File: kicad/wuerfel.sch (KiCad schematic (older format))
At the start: 18 parts, among them IC1 ATTINY13A-P

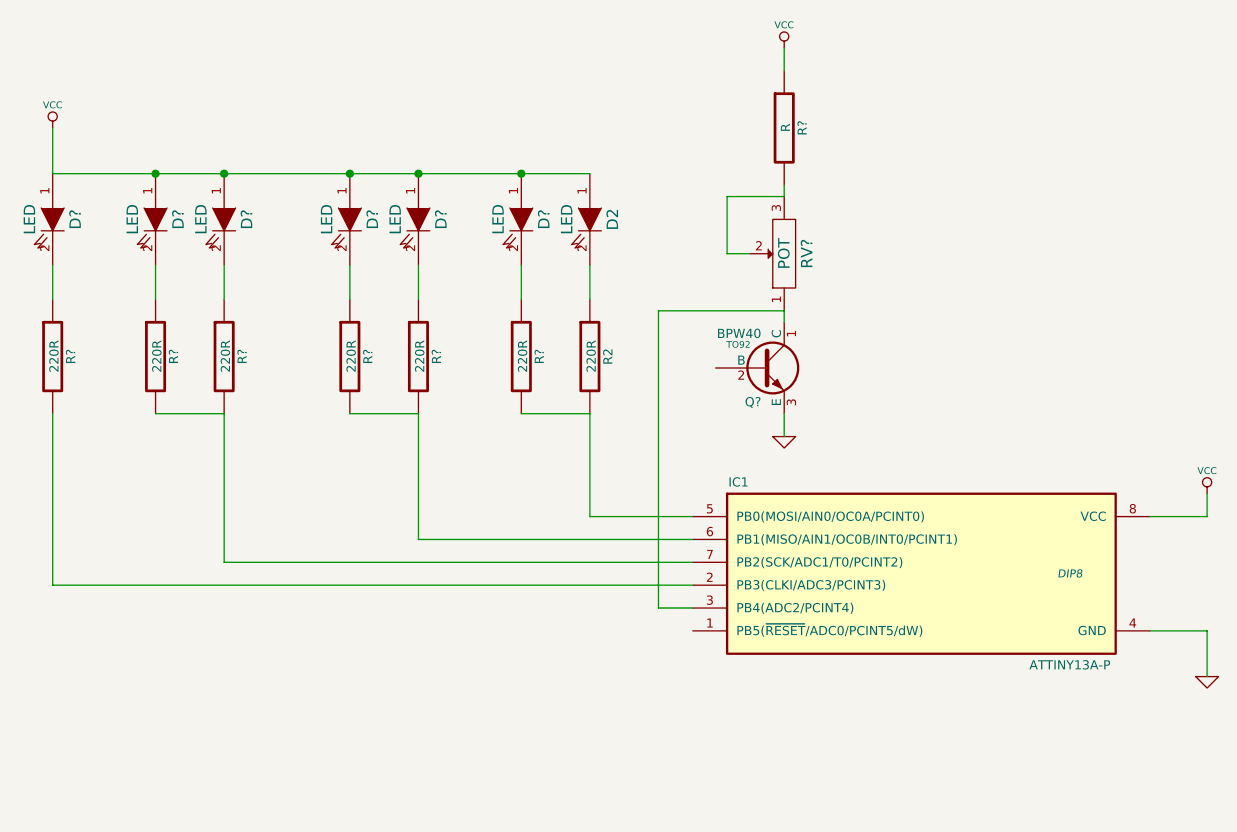
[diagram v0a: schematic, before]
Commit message: Stub für firmware angelegt, Readme erweitert
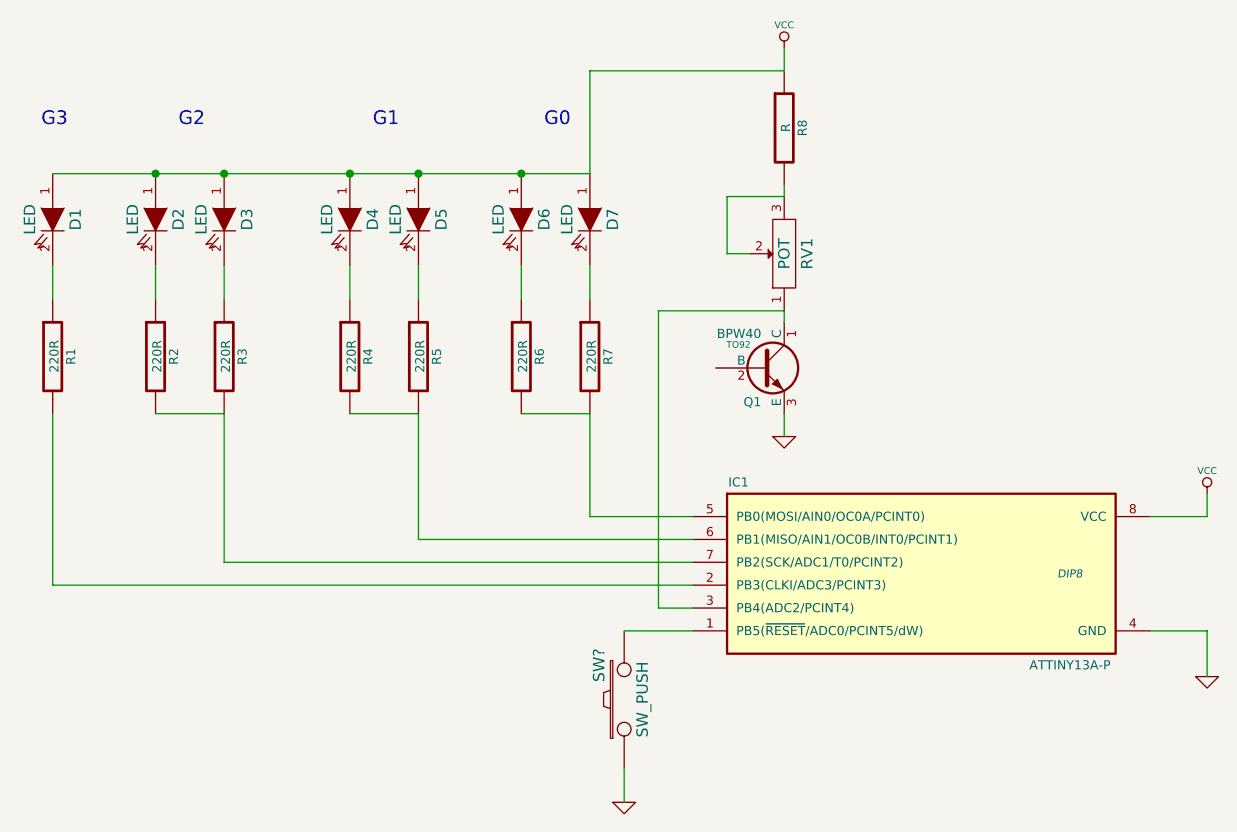
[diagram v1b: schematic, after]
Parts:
- added SW?: SW_PUSH, ~, symbol SW_PUSH
- gave numbers to parts that had none: 15
- renumbered D2 to D7, R2 to R7
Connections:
- net GND: now also SW?.1
- net at IC1.1 (PB5(~RESET~/ADC0/PCINT5/dW)): now also SW?.2
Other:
- note added: "G0"
- note added: "G1"
- note added: "G2"
- note added: "G3\n"
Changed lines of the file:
@@
 LIBS:contrib
 LIBS:valves
-LIBS:Gajda_opto
+LIBS:wuerfel-cache
 EELAYER 27 0
 EELAYER END
@@
 Sheet 1 1
 Title ""
-Date "5 jul 2015"
+Date "6 jul 2015"
 Rev ""
 Comp ""
@@
 $EndComp
 $Comp
-L LED D2
+L LED D7
 U 1 1 5599348D
 P 3900 2250
-F 0 "D2" H 3900 2350 50  0000 C CNN
+F 0 "D7" H 3900 2350 50  0000 C CNN
 F 1 "LED" H 3900 2150 50  0000 C CNN
 F 2 "~" H 3900 2250 60  0000 C CNN
@@
 $EndComp
 $Comp
-L R R2
+L R R7
 U 1 1 559934D7
 P 3900 2850
-F 0 "R2" V 3980 2850 40  0000 C CNN
+F 0 "R7" V 3980 2850 40  0000 C CNN
 F 1 "220R" V 3907 2851 40  0000 C CNN
 F 2 "~" V 3830 2850 30  0000 C CNN
@@
 $EndComp
 $Comp
-L VCC #PWR1
-U 1 1 559935EB
-P 1550 1850
-F 0 "#PWR1" H 1550 1950 30  0001 C CNN
-F 1 "VCC" H 1550 1950 30  0000 C CNN
-F 2 "" H 1550 1850 60  0000 C CNN
-F 3 "" H 1550 1850 60  0000 C CNN
-	1    1550 1850
-	1    0    0    -1
-$EndComp
-$Comp
-L GND #PWR2
+L GND #PWR4
 U 1 1 55993601
 P 6600 4250
-F 0 "#PWR2" H 6600 4250 30  0001 C CNN
+F 0 "#PWR4" H 6600 4250 30  0001 C CNN
 F 1 "GND" H 6600 4180 30  0001 C CNN
 F 2 "" H 6600 4250 60  0000 C CNN
@@
 	3900 2450 3900 2600
 $Comp
-L LED D?
+L LED D6
 U 1 1 559943D0
 P 3600 2250
-F 0 "D?" H 3600 2350 50  0000 C CNN
+F 0 "D6" H 3600 2350 50  0000 C CNN
 F 1 "LED" H 3600 2150 50  0000 C CNN
 F 2 "~" H 3600 2250 60  0000 C CNN
@@
 $EndComp
 $Comp
-L R R?
+L R R6
 U 1 1 559943D6
 P 3600 2850
-F 0 "R?" V 3680 2850 40  0000 C CNN
+F 0 "R6" V 3680 2850 40  0000 C CNN
 F 1 "220R" V 3607 2851 40  0000 C CNN
 F 2 "~" V 3530 2850 30  0000 C CNN
@@
 	3600 2450 3600 2600
 $Comp
-L LED D?
+L LED D1
 U 1 1 559943E1
 P 1550 2250
-F 0 "D?" H 1550 2350 50  0000 C CNN
+F 0 "D1" H 1550 2350 50  0000 C CNN
 F 1 "LED" H 1550 2150 50  0000 C CNN
 F 2 "~" H 1550 2250 60  0000 C CNN
@@
 $EndComp
 $Comp
-L R R?
+L R R1
 U 1 1 559943E7
 P 1550 2850
-F 0 "R?" V 1630 2850 40  0000 C CNN
+F 0 "R1" V 1630 2850 40  0000 C CNN
 F 1 "220R" V 1557 2851 40  0000 C CNN
 F 2 "~" V 1480 2850 30  0000 C CNN
@@
 	1550 2450 1550 2600
 $Comp
-L LED D?
+L LED D5
 U 1 1 559943EE
 P 3150 2250
-F 0 "D?" H 3150 2350 50  0000 C CNN
+F 0 "D5" H 3150 2350 50  0000 C CNN
 F 1 "LED" H 3150 2150 50  0000 C CNN
 F 2 "~" H 3150 2250 60  0000 C CNN
@@
 $EndComp
 $Comp
-L R R?
+L R R5
 U 1 1 559943F4
 P 3150 2850
-F 0 "R?" V 3230 2850 40  0000 C CNN
+F 0 "R5" V 3230 2850 40  0000 C CNN
 F 1 "220R" V 3157 2851 40  0000 C CNN
 F 2 "~" V 3080 2850 30  0000 C CNN
@@
 	3150 2450 3150 2600
 $Comp
-L LED D?
+L LED D4
 U 1 1 559943FB
 P 2850 2250
-F 0 "D?" H 2850 2350 50  0000 C CNN
+F 0 "D4" H 2850 2350 50  0000 C CNN
 F 1 "LED" H 2850 2150 50  0000 C CNN
 F 2 "~" H 2850 2250 60  0000 C CNN
@@
 $EndComp
 $Comp
-L R R?
+L R R4
 U 1 1 55994401
 P 2850 2850
-F 0 "R?" V 2930 2850 40  0000 C CNN
+F 0 "R4" V 2930 2850 40  0000 C CNN
 F 1 "220R" V 2857 2851 40  0000 C CNN
 F 2 "~" V 2780 2850 30  0000 C CNN
@@
 	2850 2450 2850 2600
 $Comp
-L LED D?
+L LED D3
 U 1 1 55994408
 P 2300 2250
-F 0 "D?" H 2300 2350 50  0000 C CNN
+F 0 "D3" H 2300 2350 50  0000 C CNN
 F 1 "LED" H 2300 2150 50  0000 C CNN
 F 2 "~" H 2300 2250 60  0000 C CNN
@@
 $EndComp
 $Comp
-L R R?
+L R R3
 U 1 1 5599440E
 P 2300 2850
-F 0 "R?" V 2380 2850 40  0000 C CNN
+F 0 "R3" V 2380 2850 40  0000 C CNN
 F 1 "220R" V 2307 2851 40  0000 C CNN
 F 2 "~" V 2230 2850 30  0000 C CNN
@@
 	2300 2450 2300 2600
 $Comp
-L LED D?
+L LED D2
 U 1 1 55994415
 P 2000 2250
-F 0 "D?" H 2000 2350 50  0000 C CNN
+F 0 "D2" H 2000 2350 50  0000 C CNN
 F 1 "LED" H 2000 2150 50  0000 C CNN
 F 2 "~" H 2000 2250 60  0000 C CNN
@@
 $EndComp
 $Comp
-L R R?
+L R R2
 U 1 1 5599441B
 P 2000 2850
-F 0 "R?" V 2080 2850 40  0000 C CNN
+F 0 "R2" V 2080 2850 40  0000 C CNN
 F 1 "220R" V 2007 2851 40  0000 C CNN
 F 2 "~" V 1930 2850 30  0000 C CNN
@@
 Connection ~ 3600 2050
 $Comp
-L VCC #PWR?
+L VCC #PWR3
 U 1 1 559944A0
 P 6600 3450
-F 0 "#PWR?" H 6600 3550 30  0001 C CNN
+F 0 "#PWR3" H 6600 3550 30  0001 C CNN
 F 1 "VCC" H 6600 3550 30  0000 C CNN
 F 2 "" H 6600 3450 60  0000 C CNN
@@
 Wire Wire Line
 	6600 3550 6600 3450
-Wire Wire Line
-	1550 1850 1550 2050
-$Comp
-L BC547 Q?
+$Comp
+L BC547 Q1
 U 1 1 55994683
 P 4650 2900
-F 0 "Q?" H 4650 2751 40  0000 R CNN
+F 0 "Q1" H 4650 2751 40  0000 R CNN
 F 1 "BPW40" H 4650 3050 40  0000 R CNN
 F 2 "TO92" H 4550 3002 29  0000 C CNN
@@
 $EndComp
 $Comp
-L GND #PWR?
+L GND #PWR2
 U 1 1 559946BD
 P 4750 3200
-F 0 "#PWR?" H 4750 3200 30  0001 C CNN
+F 0 "#PWR2" H 4750 3200 30  0001 C CNN
 F 1 "GND" H 4750 3130 30  0001 C CNN
 F 2 "" H 4750 3200 60  0000 C CNN
@@
 	4750 3100 4750 3200
 $Comp
-L R R?
+L R R8
 U 1 1 559946F1
 P 4750 1850
-F 0 "R?" V 4830 1850 40  0000 C CNN
+F 0 "R8" V 4830 1850 40  0000 C CNN
 F 1 "R" V 4757 1851 40  0000 C CNN
 F 2 "~" V 4680 1850 30  0000 C CNN
@@
 $EndComp
 $Comp
-L POT RV?
+L POT RV1
 U 1 1 5599470F
 P 4750 2400
-F 0 "RV?" H 4750 2300 50  0000 C CNN
+F 0 "RV1" H 4750 2300 50  0000 C CNN
 F 1 "POT" H 4750 2400 50  0000 C CNN
 F 2 "~" H 4750 2400 60  0000 C CNN
@@
 	4750 2150 4750 2100
 $Comp
-L VCC #PWR?
+L VCC #PWR1
 U 1 1 55994754
 P 4750 1500
-F 0 "#PWR?" H 4750 1600 30  0001 C CNN
+F 0 "#PWR1" H 4750 1600 30  0001 C CNN
 F 1 "VCC" H 4750 1600 30  0000 C CNN
 F 2 "" H 4750 1500 60  0000 C CNN
@@
 Wire Wire Line
 	1550 3850 4350 3850
+Wire Wire Line
+	4750 1600 3900 1600
+Wire Wire Line
+	3900 1600 3900 2050
+Text Notes 1500 1850 0    60   ~ 0
+G3\n
+Text Notes 2100 1850 0    60   ~ 0
+G2
+Text Notes 2950 1850 0    60   ~ 0
+G1
+Text Notes 3700 1850 0    60   ~ 0
+G0
+$Comp
+L SW_PUSH SW?
+U 1 1 559AB1B8
+P 4050 4350
+F 0 "SW?" H 4200 4460 50  0000 C CNN
+F 1 "SW_PUSH" H 4050 4270 50  0000 C CNN
+F 2 "~" H 4050 4350 60  0000 C CNN
+F 3 "~" H 4050 4350 60  0000 C CNN
+	1    4050 4350
+	0    -1   -1   0
+$EndComp
+$Comp
+L GND #PWR?
+U 1 1 559AB1D0
+P 4050 4800
+F 0 "#PWR?" H 4050 4800 30  0001 C CNN
+F 1 "GND" H 4050 4730 30  0001 C CNN
+F 2 "" H 4050 4800 60  0000 C CNN
+F 3 "" H 4050 4800 60  0000 C CNN
+	1    4050 4800
+	1    0    0    -1
+$EndComp
+Wire Wire Line
+	4050 4800 4050 4650
+Wire Wire Line
+	4350 4050 4050 4050
 $EndSCHEMATC

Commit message: Schalter aus Design entfernt, einfache Implementation fertiggestellt
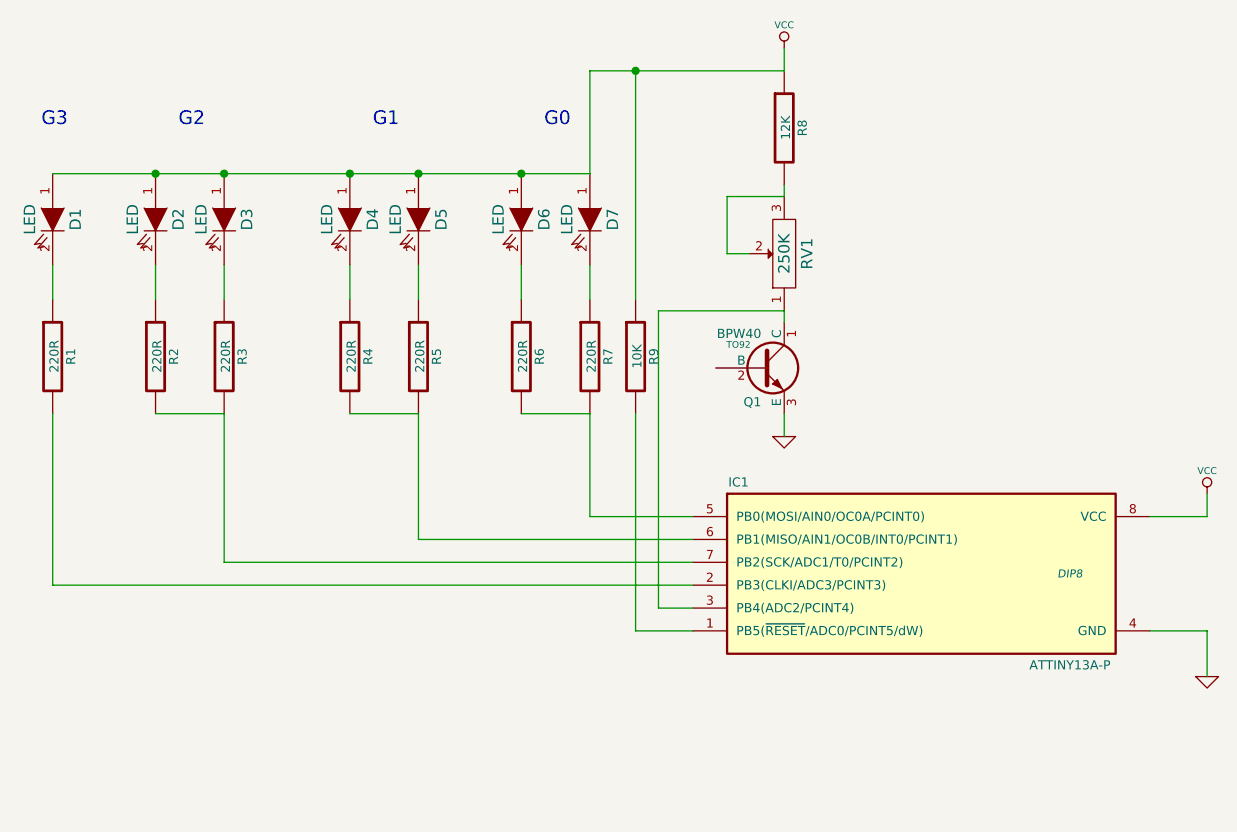
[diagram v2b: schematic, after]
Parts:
- removed SW?: SW_PUSH, ~, symbol SW_PUSH
- added R9: 10K, ~, symbol R
- R8: value R -> 12K
- RV1: value POT -> 250K
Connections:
- net VCC: now also R9.1
- net at IC1.1 (PB5(~RESET~/ADC0/PCINT5/dW)): now also R9.2
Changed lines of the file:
@@
 Sheet 1 1
 Title ""
-Date "6 jul 2015"
+Date "19 jul 2015"
 Rev ""
 Comp ""
@@
 	1    0    0    -1
 $EndComp
-Wire Wire Line
-	6350 4050 6600 4050
-Wire Wire Line
-	6600 4050 6600 4250
-Wire Wire Line
-	3900 2450 3900 2600
 $Comp
 L LED D6
@@
 	1    0    0    -1
 $EndComp
-Wire Wire Line
-	3600 2450 3600 2600
 $Comp
 L LED D1
@@
 	1    0    0    -1
 $EndComp
-Wire Wire Line
-	1550 2450 1550 2600
 $Comp
 L LED D5
@@
 	1    0    0    -1
 $EndComp
-Wire Wire Line
-	3150 2450 3150 2600
 $Comp
 L LED D4
@@
 	1    0    0    -1
 $EndComp
-Wire Wire Line
-	2850 2450 2850 2600
 $Comp
 L LED D3
@@
 	1    0    0    -1
 $EndComp
-Wire Wire Line
-	2300 2450 2300 2600
 $Comp
 L LED D2
@@
 	1    0    0    -1
 $EndComp
-Wire Wire Line
-	2000 2450 2000 2600
-Wire Wire Line
-	2000 3100 2300 3100
-Wire Wire Line
-	2850 3100 3150 3100
-Wire Wire Line
-	3600 3100 3900 3100
-Wire Wire Line
-	1550 2050 3900 2050
-Connection ~ 2000 2050
-Connection ~ 2300 2050
-Connection ~ 2850 2050
-Connection ~ 3150 2050
-Connection ~ 3600 2050
 $Comp
 L VCC #PWR3
@@
 	1    0    0    -1
 $EndComp
-Wire Wire Line
-	6350 3550 6600 3550
-Wire Wire Line
-	6600 3550 6600 3450
 $Comp
 L BC547 Q1
@@
 	1    0    0    -1
 $EndComp
-Wire Wire Line
-	4750 3100 4750 3200
 $Comp
 L R R8
@@
 P 4750 1850
 F 0 "R8" V 4830 1850 40  0000 C CNN
-F 1 "R" V 4757 1851 40  0000 C CNN
+F 1 "12K" V 4757 1851 40  0000 C CNN
 F 2 "~" V 4680 1850 30  0000 C CNN
 F 3 "~" H 4750 1850 30  0000 C CNN
@@
 P 4750 2400
 F 0 "RV1" H 4750 2300 50  0000 C CNN
-F 1 "POT" H 4750 2400 50  0000 C CNN
+F 1 "250K" H 4750 2400 50  0000 C CNN
 F 2 "~" H 4750 2400 60  0000 C CNN
 F 3 "~" H 4750 2400 60  0000 C CNN
@@
 	0    -1   -1   0
 $EndComp
-Wire Wire Line
-	4600 2400 4500 2400
-Wire Wire Line
-	4500 2400 4500 2150
-Wire Wire Line
-	4500 2150 4750 2150
-Wire Wire Line
-	4750 2150 4750 2100
 $Comp
 L VCC #PWR1
@@
 	1    0    0    -1
 $EndComp
-Wire Wire Line
-	4750 1500 4750 1600
-Wire Wire Line
-	4750 2650 4750 2700
-Wire Wire Line
-	4750 2650 4200 2650
-Wire Wire Line
-	4200 2650 4200 3950
-Wire Wire Line
-	4200 3950 4350 3950
-Wire Wire Line
-	3900 3100 3900 3550
-Wire Wire Line
-	3900 3550 4350 3550
-Wire Wire Line
-	3150 3100 3150 3650
-Wire Wire Line
-	3150 3650 4350 3650
-Wire Wire Line
-	2300 3100 2300 3750
-Wire Wire Line
-	2300 3750 4350 3750
-Wire Wire Line
-	1550 3100 1550 3850
-Wire Wire Line
-	1550 3850 4350 3850
-Wire Wire Line
-	4750 1600 3900 1600
-Wire Wire Line
-	3900 1600 3900 2050
 Text Notes 1500 1850 0    60   ~ 0
 G3\n
@@
 G0
 $Comp
-L SW_PUSH SW?
-U 1 1 559AB1B8
-P 4050 4350
-F 0 "SW?" H 4200 4460 50  0000 C CNN
-F 1 "SW_PUSH" H 4050 4270 50  0000 C CNN
-F 2 "~" H 4050 4350 60  0000 C CNN
-F 3 "~" H 4050 4350 60  0000 C CNN
-	1    4050 4350
-	0    -1   -1   0
-$EndComp
-$Comp
-L GND #PWR?
-U 1 1 559AB1D0
-P 4050 4800
-F 0 "#PWR?" H 4050 4800 30  0001 C CNN
-F 1 "GND" H 4050 4730 30  0001 C CNN
-F 2 "" H 4050 4800 60  0000 C CNN
-F 3 "" H 4050 4800 60  0000 C CNN
-	1    4050 4800
-	1    0    0    -1
-$EndComp
-Wire Wire Line
-	4050 4800 4050 4650
-Wire Wire Line
-	4350 4050 4050 4050
+L R R9
+U 1 1 55AB861B
+P 4100 2850
+F 0 "R9" V 4180 2850 40  0000 C CNN
+F 1 "10K" V 4107 2851 40  0000 C CNN
+F 2 "~" V 4030 2850 30  0000 C CNN
+F 3 "~" H 4100 2850 30  0000 C CNN
+	1    4100 2850
+	1    0    0    -1
+$EndComp
+Wire Wire Line
+	6350 4050 6600 4050
+Wire Wire Line
+	6600 4050 6600 4250
+Wire Wire Line
+	3900 2450 3900 2600
+Wire Wire Line
+	3600 2450 3600 2600
+Wire Wire Line
+	1550 2450 1550 2600
+Wire Wire Line
+	3150 2450 3150 2600
+Wire Wire Line
+	2850 2450 2850 2600
+Wire Wire Line
+	2300 2450 2300 2600
+Wire Wire Line
+	2000 2450 2000 2600
+Wire Wire Line
+	2000 3100 2300 3100
+Wire Wire Line
+	2850 3100 3150 3100
+Wire Wire Line
+	3600 3100 3900 3100
+Wire Wire Line
+	1550 2050 3900 2050
+Connection ~ 2000 2050
+Connection ~ 2300 2050
+Connection ~ 2850 2050
+Connection ~ 3150 2050
+Connection ~ 3600 2050
+Wire Wire Line
+	6350 3550 6600 3550
+Wire Wire Line
+	6600 3550 6600 3450
+Wire Wire Line
+	4750 3100 4750 3200
+Wire Wire Line
+	4600 2400 4500 2400
+Wire Wire Line
+	4500 2400 4500 2150
+Wire Wire Line
+	4500 2150 4750 2150
+Wire Wire Line
+	4750 2150 4750 2100
+Wire Wire Line
+	4750 1500 4750 1600
+Wire Wire Line
+	4750 2650 4750 2700
+Wire Wire Line
+	4750 2650 4200 2650
+Wire Wire Line
+	4200 2650 4200 3950
+Wire Wire Line
+	4200 3950 4350 3950
+Wire Wire Line
+	3900 3100 3900 3550
+Wire Wire Line
+	3900 3550 4350 3550
+Wire Wire Line
+	3150 3100 3150 3650
+Wire Wire Line
+	3150 3650 4350 3650
+Wire Wire Line
+	2300 3100 2300 3750
+Wire Wire Line
+	2300 3750 4350 3750
+Wire Wire Line
+	1550 3100 1550 3850
+Wire Wire Line
+	1550 3850 4350 3850
+Wire Wire Line
+	4750 1600 3900 1600
+Wire Wire Line
+	3900 1600 3900 2050
+Wire Wire Line
+	4100 3100 4100 4050
+Wire Wire Line
+	4100 4050 4350 4050
+Wire Wire Line
+	4100 2600 4100 1600
+Connection ~ 4100 1600
 $EndSCHEMATC
